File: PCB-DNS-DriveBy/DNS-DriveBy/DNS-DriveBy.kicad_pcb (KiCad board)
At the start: 2 copper layers, 76 x 40 mm, 24 parts, among them J1 JST 2.0, J2 Conn_01x04, J3 Conn_01x03, Q1 2N3904, Q2 2N3904, SW1 SW_SPST, U1 D1 Mini, U2 NEO-6M

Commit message: publish v1.3 design files
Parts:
- added Antenna: SMA Antenna, Connector_Coaxial:SMA_Amphenol_901-144_Vertical, F.Cu at (72.4, 10.6)
- added J1: JST 2.0, Connector_JST:JST_PH_S2B-PH-SM4-TB_1x02-1MP_P2.00mm_Horizontal, B.Cu at (71.4, 29.8)
- added J4: Micro_SD_Card_Det, DNS-DriveBy:MicroSD, B.Cu at (53.1, 15.3)
- added R3: 10K, Resistor_THT:R_Axial_DIN0207_L6.3mm_D2.5mm_P7.62mm_Horizontal, F.Cu at (21.0, 21.8)
- J2: value Conn_01x04 -> SH1106
- moved JP5 65.2 mm to (4.21, 14.6)
- moved SW1 64.6 mm to (3.75, 9.96)
- moved Q2 19.6 mm to (9.46, 32.1)
- moved R4 18.0 mm to (20.9, 31.9), turned to 90 degrees
- moved Q1 16.3 mm to (9.56, 24.3), turned to 90 degrees
- moved J2 12.4 mm to (16.1, 3.61)
- moved R1 9.26 mm to (17.6, 21.9)
- moved R2 9.21 mm to (17.6, 24.3)
- moved R6 1.48 mm to (70.4, 17.1)
- moved J3 1.44 mm to (74.3, 23.4)
- moved JP4 1.40 mm to (67.0, 20.7)
- moved R5 1.40 mm to (67.0, 24.6)
- moved Ref** 1.34 mm to (38.8, 21.0)
- moved J1 0.93 mm to (71.8, 29.8)
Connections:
- J1 pad 1: Net-(J1-Pad1) -> +BATT
- J1 pad 2: +BATT -> Net-(J1-Pad2)
- J2 pad 1: GND -> +3V3
- J2 pad 2: +3V3 -> GND
- JP1 pad 1: +BATT -> GND
- JP1 pad 2: Net-(JP1-Pad2) -> Net-(U2-Pad4)
- JP5 pad 2: Net-(J1-Pad1) -> Net-(J1-Pad2)
- Q2 pad 1: Net-(JP1-Pad3) -> GND
- Q2 pad 3: +BATT -> Net-(JP1-Pad3)
- SW1 pad 2: Net-(J1-Pad1) -> Net-(J1-Pad2)
- U2 pad 1: Net-(JP1-Pad2) -> +BATT
- U2 pad 4: GND -> Net-(U2-Pad4)
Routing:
- net Net-(J1-Pad2): track 0.00 -> 111.7 mm, vias 0 -> 1
- net SS: track 0.00 -> 62.2 mm, vias 0 -> 2
- net MISO: track 0.00 -> 59.4 mm, vias 0 -> 2
- net MOSI: track 0.00 -> 59.3 mm, vias 0 -> 2
- net SCK: track 0.00 -> 54.7 mm, vias 0 -> 2
- net +BATT: track 125.4 -> 80.9 mm
- net +3V3: track 109.8 -> 153.9 mm, vias 0 -> 1
- net Net-(JP1-Pad3): track 72.0 -> 45.0 mm
- net Net-(J1-Pad1): track 25.7 -> 0.00 mm
- net GPS-EN: track 46.3 -> 29.5 mm
- net Net-(U2-Pad4): track 0.00 -> 13.3 mm
- net SCL: track 16.7 -> 29.2 mm
- net Net-(Q1-Pad2): track 7.68 -> 15.2 mm
- net Net-(JP1-Pad2): track 5.70 -> 0.00 mm
- net D4: track 63.4 -> 58.6 mm
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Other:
- board text added: "128x64 OLED"
- board text added: "GPS Low-Power"
- board text added: "JST PH"
- board text added: "LiPo Switch"
- board text added: "MicroSD"
- board text added: "Resistor Bypass"
- board text added: "Serial1"
- board text added: "Switch Bypass"
- board text added: "v1.3"
- board text removed: "JST 2.0"
- board text removed: "SSD1306 / SH1106"
- board text removed: "Serial"
- board text removed: "v1.2"

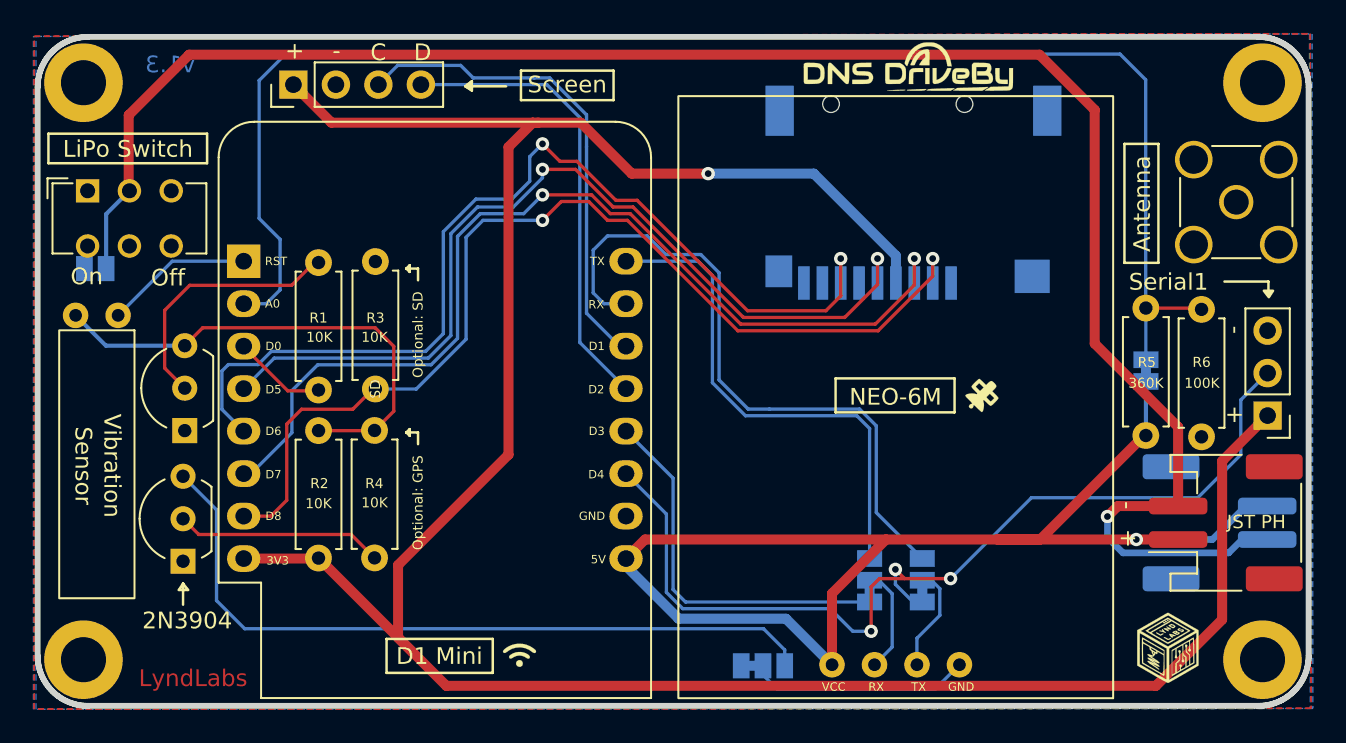
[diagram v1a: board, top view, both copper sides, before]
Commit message: update jumper pad position
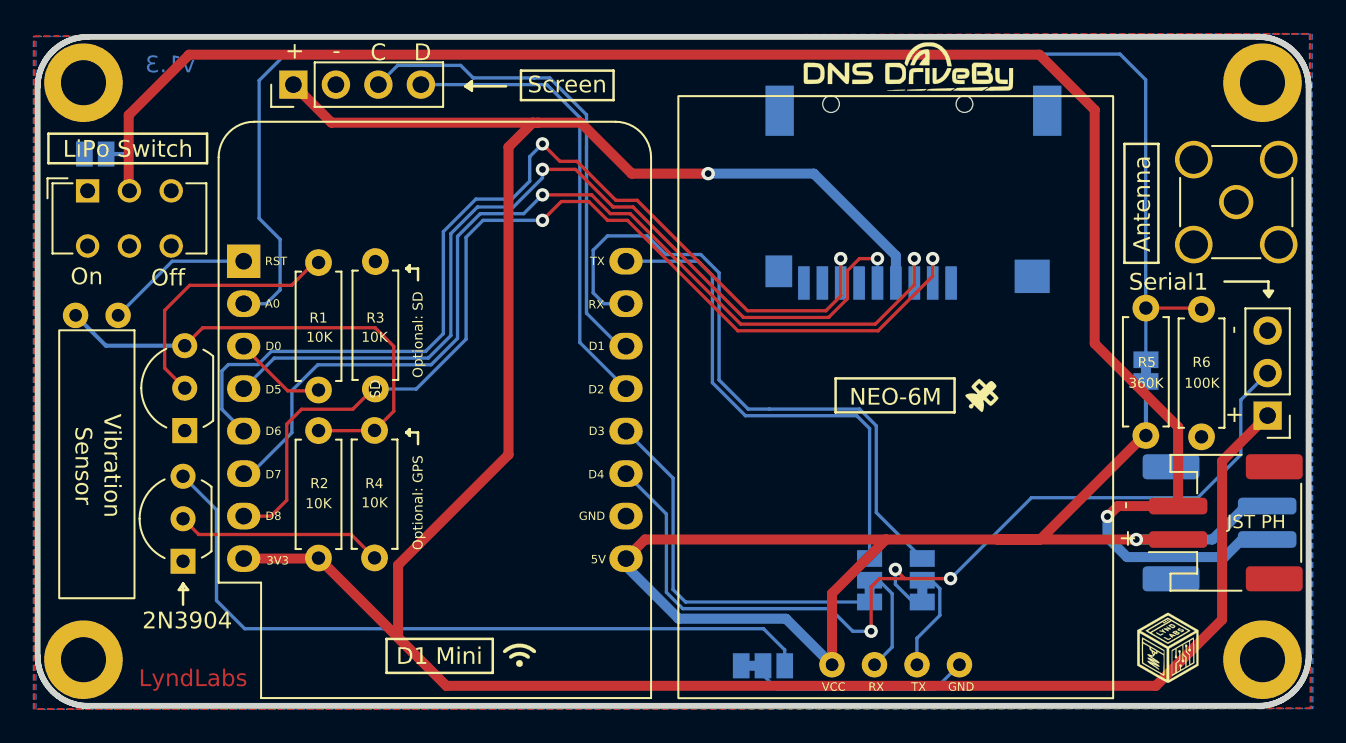
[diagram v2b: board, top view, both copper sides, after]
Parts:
- moved JP5 6.85 mm to (4.21, 7.76)
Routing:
- net Net-(J1-Pad2): track 111.7 -> 110.0 mm
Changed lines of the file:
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@@
   )
   (footprint "Jumper:SolderJumper-2_P1.3mm_Open_Pad1.0x1.5mm" (layer "B.Cu")
-    (at 4.2052 14.6132)
+    (at 4.2052 7.7632)
     (descr "SMD Solder Jumper, 1x1.5mm Pads, 0.3mm gap, open")
     (tags "solder jumper open")
@@
     (property "Sheetname" "")
     (attr exclude_from_pos_files)
-    (fp_text reference "JP5" (at 2.7 -0.4) (layer "B.SilkS")
+    (fp_text reference "JP5" (at -2.35 0.1) (layer "B.SilkS")
       (effects (font (size 0.6 0.6) (thickness 0.15)) (justify mirror))
     )
@@
     )
   )
-  (gr_line (start 6.2052 15.3257) (end 6.4802 15.0257) (layer "B.SilkS") (width 0.15))
-  (gr_line (start 6.4802 15.6007) (end 6.2052 15.3257) (layer "B.SilkS") (width 0.15))
+  (gr_line (start 6.1552 7.7757) (end 6.4302 7.4757) (layer "B.SilkS") (width 0.15))
+  (gr_line (start 6.4302 8.0507) (end 6.1552 7.7757) (layer "B.SilkS") (width 0.15))
   (gr_rect (start 14.5432 7.5792) (end 25.2552 5.5472) (layer "B.SilkS") (width 0.15) (fill none))
   (gr_rect (start 49.3982 19.4362) (end 56.5102 17.4042) (layer "B.SilkS") (width 0.15) (fill none))
@@
   (gr_line (start 51.3552 37.7382) (end 51.8302 37.2632) (layer "B.SilkS") (width 0.15))
   (gr_line (start 51.8302 33.5882) (end 51.5552 33.3632) (layer "B.SilkS") (width 0.15))
-  (gr_line (start 7.0052 18.6132) (end 7.0052 15.3132) (layer "B.SilkS") (width 0.15))
-  (gr_line (start 6.4802 15.0257) (end 6.4802 15.6007) (layer "B.SilkS") (width 0.15))
-  (gr_rect (start 1.7432 22.9042) (end 7.4802 19.2222) (layer "B.SilkS") (width 0.15) (fill none))
+  (gr_line (start 6.4302 7.4757) (end 6.4302 8.0507) (layer "B.SilkS") (width 0.15))
+  (gr_rect (start 7.2682 8.4542) (end 13.0052 4.7722) (layer "B.SilkS") (width 0.15) (fill none))
   (gr_line (start 52.3677 33.5757) (end 52.6302 33.3382) (layer "B.SilkS") (width 0.15))
   (gr_line (start 52.3677 37.2507) (end 52.3677 33.5757) (layer "B.SilkS") (width 0.15))
   (gr_rect (start 28.3432 39.3292) (end 41.3052 37.2972) (layer "B.SilkS") (width 0.15) (fill none))
   (gr_line (start 52.65 32.6) (end 54.65 32.6) (layer "B.SilkS") (width 0.15))
-  (gr_line (start 7.0052 15.3132) (end 6.2052 15.3132) (layer "B.SilkS") (width 0.15))
+  (gr_line (start 6.9552 7.7632) (end 6.1552 7.7632) (layer "B.SilkS") (width 0.15))
   (gr_rect (start 58.6432 22.1167) (end 65.5552 18.4347) (layer "B.SilkS") (width 0.15) (fill none))
   (gr_line (start 49.5 32.6) (end 51.5 32.6) (layer "B.SilkS") (width 0.15))
@@
     (effects (font (size 1 1) (thickness 0.15)) (justify mirror))
   )
-  (gr_text "Switch\nBypass" (at 4.6302 20.9132) (layer "B.SilkS")
+  (gr_text "Switch\nBypass" (at 10.1552 6.4632) (layer "B.SilkS")
     (effects (font (size 1 1) (thickness 0.15)) (justify mirror))
   )
@@
   (segment (start 48.26 38.3012) (end 48.26 34.0404) (width 0.6) (layer "F.Cu") (net 1))
   (via (at 66.4552 30.8132) (size 0.8) (drill 0.4) (layers "F.Cu" "B.Cu") (net 1))
-  (segment (start 66.4552 30.8132) (end 71.0052 30.8132) (width 0.4) (layer "B.Cu") (net 1))
+  (segment (start 73.0052 28.8132) (end 74.2802 28.8132) (width 0.6) (layer "B.Cu") (net 1))
   (segment (start 45.507839 35.549039) (end 48.26 38.3012) (width 0.6) (layer "B.Cu") (net 1))
-  (segment (start 73.0052 28.8132) (end 74.2802 28.8132) (width 0.4) (layer "B.Cu") (net 1))
+  (segment (start 66.4552 30.8132) (end 71.0052 30.8132) (width 0.6) (layer "B.Cu") (net 1))
+  (segment (start 71.0052 30.8132) (end 73.0052 28.8132) (width 0.6) (layer "B.Cu") (net 1))
   (segment (start 39.086184 35.549039) (end 45.507839 35.549039) (width 0.6) (layer "B.Cu") (net 1))
   (segment (start 67.0314 24.5898) (end 67.0262 24.595) (width 0.25) (layer "B.Cu") (net 1))
@@
   (segment (start 35.941 31.9532) (end 35.941 32.403855) (width 0.6) (layer "B.Cu") (net 1))
   (segment (start 67.0314 21.3632) (end 67.0314 24.5898) (width 0.25) (layer "B.Cu") (net 1))
-  (segment (start 71.0052 30.8132) (end 73.0052 28.8132) (width 0.4) (layer "B.Cu") (net 1))
   (segment (start 67.0262 16.975) (end 70.4552 16.975) (width 0.2) (layer "F.Cu") (net 3))
   (segment (start 15.2552 12.8632) (end 15.2552 15.8882) (width 0.2) (layer "B.Cu") (net 3))
@@
   (segment (start 63.9672 19.0952) (end 68.9552 24.0832) (width 0.6) (layer "F.Cu") (net 7))
   (via (at 64.7302 29.4382) (size 0.8) (drill 0.4) (layers "F.Cu" "B.Cu") (net 7))
-  (segment (start 71.980689 31.612711) (end 65.654711 31.612711) (width 0.4) (layer "B.Cu") (net 7))
-  (segment (start 72.7802 30.8132) (end 71.980689 31.612711) (width 0.4) (layer "B.Cu") (net 7))
-  (segment (start 64.7302 30.6882) (end 64.7302 29.4382) (width 0.4) (layer "B.Cu") (net 7))
-  (segment (start 74.2802 30.8132) (end 72.7802 30.8132) (width 0.4) (layer "B.Cu") (net 7))
-  (segment (start 4.8552 11.3557) (end 6.2477 9.9632) (width 0.25) (layer "B.Cu") (net 7))
-  (segment (start 65.654711 31.612711) (end 64.7302 30.6882) (width 0.4) (layer "B.Cu") (net 7))
-  (segment (start 4.8552 14.6132) (end 4.8552 11.3557) (width 0.25) (layer "B.Cu") (net 7))
+  (segment (start 65.9052 31.8632) (end 64.7302 30.6882) (width 0.6) (layer "B.Cu") (net 7))
+  (segment (start 74.2802 30.8132) (end 72.7802 30.8132) (width 0.6) (layer "B.Cu") (net 7))
+  (segment (start 6.2477 8.1557) (end 5.8552 7.7632) (width 0.25) (layer "B.Cu") (net 7))
+  (segment (start 64.7302 30.6882) (end 64.7302 29.4382) (width 0.6) (layer "B.Cu") (net 7))
+  (segment (start 71.7302 31.8632) (end 65.9052 31.8632) (width 0.6) (layer "B.Cu") (net 7))
+  (segment (start 5.8552 7.7632) (end 4.8552 7.7632) (width 0.25) (layer "B.Cu") (net 7))
+  (segment (start 6.2477 9.9632) (end 6.2477 8.1557) (width 0.25) (layer "B.Cu") (net 7))
+  (segment (start 72.7802 30.8132) (end 71.7302 31.8632) (width 0.6) (layer "B.Cu") (net 7))
   (segment (start 8.8072 14.1732) (end 13.081 14.1732) (width 0.2) (layer "B.Cu") (net 8))
   (segment (start 5.57 17.4104) (end 8.8072 14.1732) (width 0.2) (layer "B.Cu") (net 8))
@@
   (segment (start 31.2132 3.6132) (end 23.6752 3.6132) (width 0.2) (layer "B.Cu") (net 14))
   (segment (start 33.18048 5.58048) (end 31.2132 3.6132) (width 0.2) (layer "B.Cu") (net 14))
-  (segment (start 49.01824 17.53416) (end 50.9802 15.5722) (width 0.2) (layer "F.Cu") (net 15))
-  (segment (start 42.962172 17.53416) (end 49.01824 17.53416) (width 0.2) (layer "F.Cu") (net 15))
+  (segment (start 42.962172 17.53416) (end 48.059247 17.534159) (width 0.2) (layer "F.Cu") (net 15))
+  (segment (start 35.171156 10.930162) (end 36.358174 10.930162) (width 0.2) (layer "F.Cu") (net 15))
+  (segment (start 48.059247 17.534159) (end 49.17972 16.413686) (width 0.2) (layer "F.Cu") (net 15))
+  (segment (start 30.9472 8.6812) (end 32.922194 8.6812) (width 0.2) (layer "F.Cu") (net 15))
+  (segment (start 49.17972 16.413686) (end 49.17972 14.73868) (width 0.2) (layer "F.Cu") (net 15))
+  (segment (start 49.9032 14.0152) (end 50.9802 14.0152) (width 0.2) (layer "F.Cu") (net 15))
+  (segment (start 49.17972 14.73868) (end 49.9032 14.0152) (width 0.2) (layer "F.Cu") (net 15))
   (segment (start 36.358174 10.930162) (end 42.962172 17.53416) (width 0.2) (layer "F.Cu") (net 15))
-  (segment (start 50.9802 15.5722) (end 50.9802 14.0152) (width 0.2) (layer "F.Cu") (net 15))
-  (segment (start 30.9472 8.6812) (end 32.922194 8.6812) (width 0.2) (layer "F.Cu") (net 15))
   (segment (start 32.922194 8.6812) (end 35.171156 10.930162) (width 0.2) (layer "F.Cu") (net 15))
-  (segment (start 35.171156 10.930162) (end 36.358174 10.930162) (width 0.2) (layer "F.Cu") (net 15))
   (via (at 50.9802 14.0152) (size 0.8) (drill 0.4) (layers "F.Cu" "B.Cu") (net 15))
   (via (at 30.9472 8.6812) (size 0.8) (drill 0.4) (layers "F.Cu" "B.Cu") (net 15))
